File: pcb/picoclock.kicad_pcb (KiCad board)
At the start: 2 copper layers, 175.8 x 64 mm, 58 parts, among them J1 UART, J10 USB, J11 Alt Power, J12 PWM, J2 AUDIO, J3 xx, J4 xx, J6 USB_C_Receptacle, J7 xx, J8 xx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

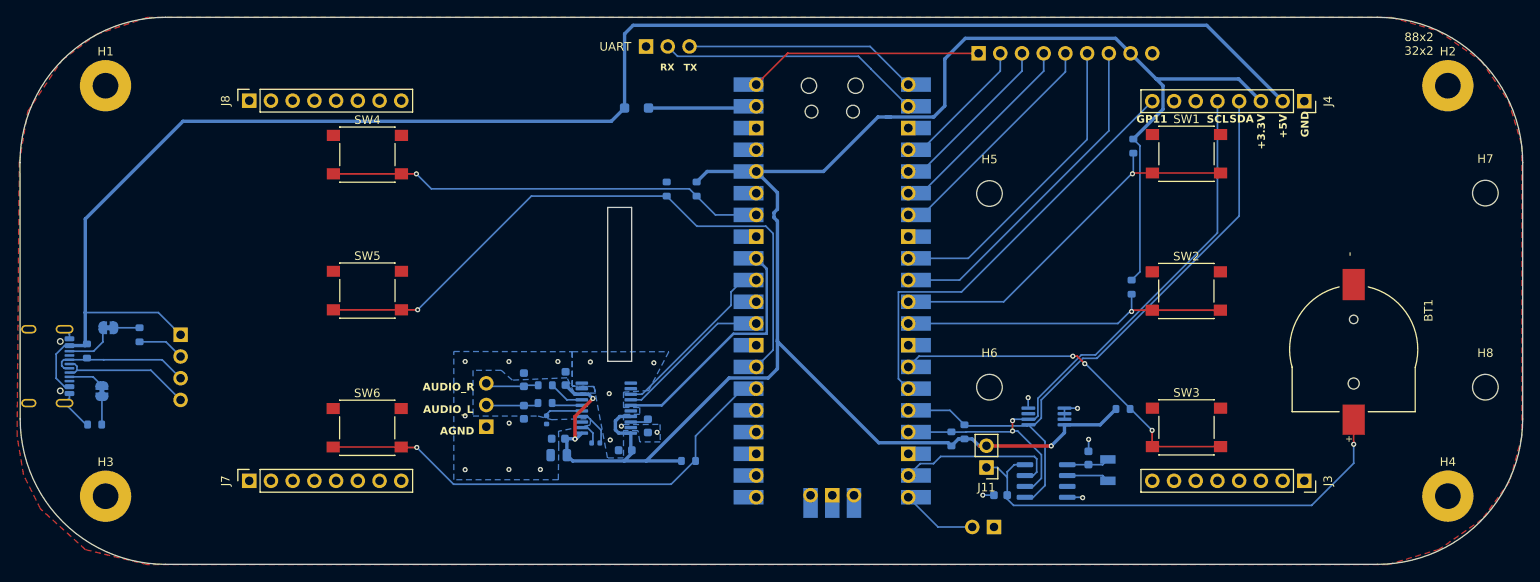
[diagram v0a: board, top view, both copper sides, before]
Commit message: [pcb] new GPIO arrangement
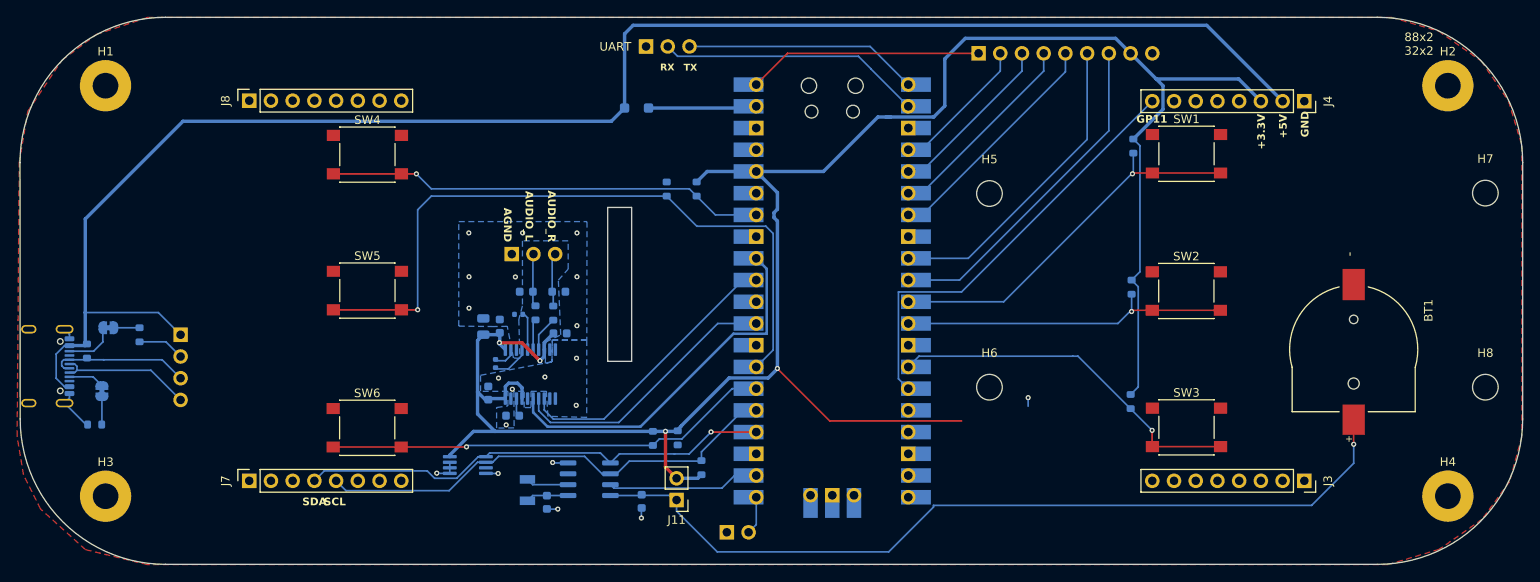
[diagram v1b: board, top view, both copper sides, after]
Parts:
- moved Y1 67.9 mm to (118.2, 122.2), turned to 90 degrees
- moved U3 67.9 mm to (111.3, 119.3), turned to 180 degrees
- moved C1 63.5 mm to (120.5, 123.6), turned to 90 degrees
- moved U1 53.4 mm to (125.5, 120.9), turned to 0 degrees
- moved C2 42.0 mm to (131.6, 123.5), turned to -90 degrees
- moved J11 36.4 mm to (135.7, 123.3)
- moved R1 33.5 mm to (135.8, 116.1), turned to -90 degrees
- moved J12 31.3 mm to (141.6, 127.1), turned to -90 degrees
- moved R3 29.4 mm to (138.6, 119.6)
- moved J2 20.4 mm to (116.4, 94.6), turned to -90 degrees
- moved C6 17.4 mm to (113.1, 103.1), turned to 90 degrees
- moved C3 17.4 mm to (113.7, 110.8), turned to -90 degrees
- moved C9 15.9 mm to (116.5, 113.5), turned to 180 degrees
- moved C7 15.0 mm to (114.5, 107.4), turned to -90 degrees
- moved C4 14.8 mm to (115.0, 103.0), turned to -90 degrees
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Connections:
- net GPIO10 renamed GPIO10/btn
- net GPIO11 renamed GPIO11/led
- net GPIO8 renamed GPIO8/btn
- net GPIO9 renamed GPIO9/btn
- J12 pad 2: GPIO15 / PWM -> GPIO16 / PWM
- J4 pad 4: SDA -> unconnected-(J4-Pin_4-Pad4)
- J4 pad 5: SCL -> unconnected-(J4-Pin_5-Pad5)
- J7 pad 4: unconnected-(J7-Pin_4-Pad4) -> SDA
- J7 pad 5: unconnected-(J7-Pin_5-Pad5) -> SCL
- U2 pad 16: SDA -> SD_D0_MISO
- U2 pad 17: SCL -> SD_D3_CS
- U2 pad 19: SQW -> SD_CLK
- U2 pad 20: GPIO15 / PWM -> SD_CMD_MOSI
- U2 pad 21: SD_D0_MISO -> GPIO16 / PWM
- U2 pad 22: SD_D3_CS -> SQW
- U2 pad 24: SD_CLK -> SDA
- U2 pad 25: SD_CMD_MOSI -> SCL
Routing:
- net 3V BATT: track 56.6 -> 100.1 mm
- net +3.3V: track 234.1 -> 255.1 mm, vias 3 -> 4
- net SDA: track 75.1 -> 55.8 mm, vias 0 -> 1
- net SCL: track 72.7 -> 55.8 mm, vias 2 -> 0
- net LRCK: track 28.7 -> 43.4 mm
- net DIN: track 18.4 -> 32.2 mm
- net BCK: track 21.1 -> 33.3 mm
- net GPIO15 / PWM: track 8.93 -> 0.00 mm
- net GPIO21/btn: track 75.4 -> 82.2 mm
- net GPIO20/btn: track 57.5 -> 52.3 mm
- net GPIO16 / PWM: track 0.00 -> 4.47 mm
- net SD_D3_CS: track 1.19 -> 0.00 mm
- net GND: track 20.3 -> 21.4 mm, vias 19 -> 20
- net GPIO10/btn: vias 3 -> 1

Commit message: [pcb] add sdcard, audio amplifier
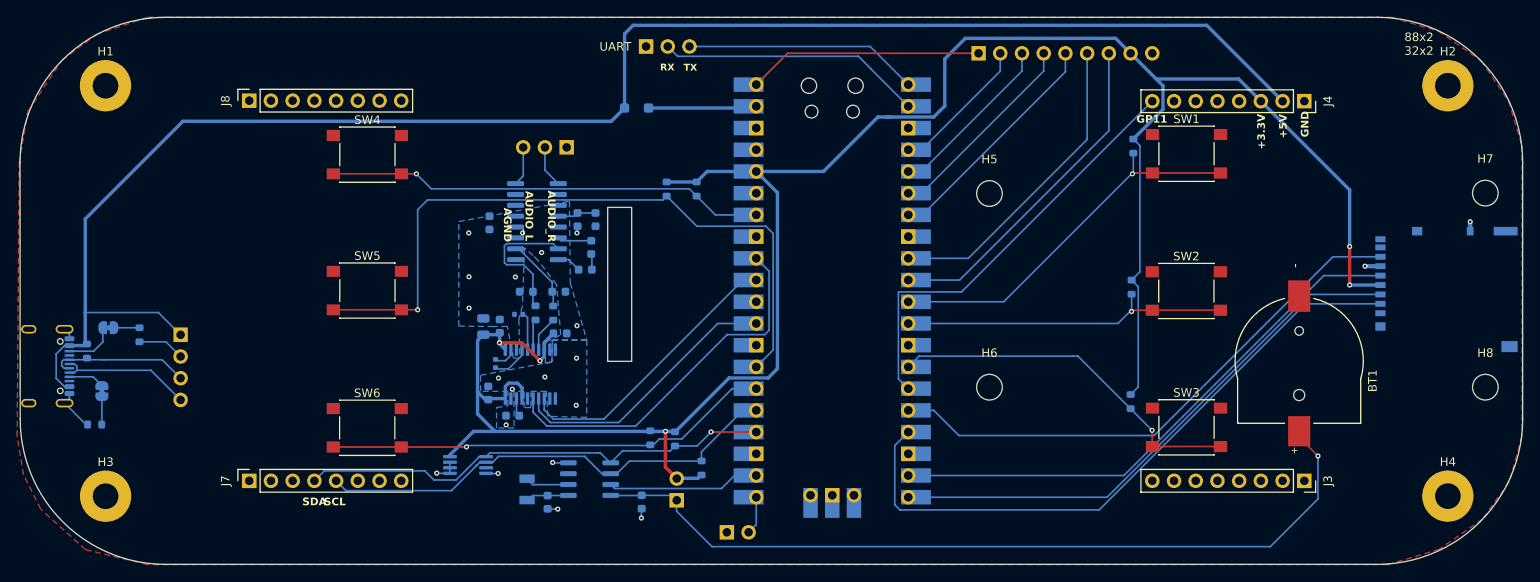
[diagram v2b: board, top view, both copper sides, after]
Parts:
- added C12: 0.1uF, Capacitor_SMD:C_0603_1608Metric, B.Cu at (125.0, 96.4)
- added C13: 1uF, Capacitor_SMD:C_0603_1608Metric, B.Cu at (125.7, 93.8)
- added C14: 1uF, Capacitor_SMD:C_0603_1608Metric, B.Cu at (113.8, 90.9)
- added C15: 1uF, Capacitor_SMD:C_0603_1608Metric, B.Cu at (126.2, 90.5)
- added C16: 470uF, Capacitor_SMD:C_0603_1608Metric, B.Cu at (124.1, 90.5)
- added J5: Micro_SD_Card_Det1, Connector_Card:microSD_HC_Hirose_DM3AT-SF-PEJM5, B.Cu at (225.7, 98.7)
- added U5: PAM8403D, Package_SO:SOP-16_3.9x9.9mm_P1.27mm, B.Cu at (119.3, 90.8)
- J11: moved to B.Cu
- moved J2 14.0 mm to (122.8, 82.1), turned to 90 degrees
- moved BT1 6.52 mm to (208.5, 107.1)
- moved R1 0.33 mm to (135.5, 116.2)
- moved R11 0.32 mm to (132.6, 116.1)
- moved Y1 0.09 mm to (118.2, 122.1)
- moved C1 0.09 mm to (120.6, 123.6)
- moved C2 0.08 mm to (131.6, 123.6)
- turned J11 to 0 degrees
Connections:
- C10 pad 2: WTAUDIO_L -> LINE_OUT_LEFT
- C11 pad 2: WTAUDIO_R -> LINE_OUT_RIGHT
- R2 pad 2: WTAUDIO_L -> LINE_OUT_LEFT
- R4 pad 2: WTAUDIO_R -> LINE_OUT_RIGHT
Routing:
- net SD_D3_CS: track 0.00 -> 76.2 mm
- net SD_D0_MISO: track 0.00 -> 65.4 mm
- net SD_CMD_MOSI: track 0.00 -> 65.0 mm
- net SD_CLK: track 0.00 -> 64.9 mm
- net LINE_OUT_LEFT: track 0.00 -> 16.7 mm
- net +3.3V: track 255.1 -> 265.5 mm, vias 4 -> 5
- net LINE_OUT_RIGHT: track 0.00 -> 8.74 mm
- net Net-(C14-Pad1): track 0.00 -> 4.51 mm
- net Net-(U5-VDD): track 0.00 -> 3.99 mm
- net 3V BATT: track 100.1 -> 97.2 mm
- net Net-(U5-VREF): track 0.00 -> 2.86 mm
- net GND: track 21.4 -> 23.6 mm, vias 20 -> 21
- net WTAUDIO_R: track 6.27 -> 4.61 mm
- net WTAUDIO_L: track 6.14 -> 4.89 mm

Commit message: [pcb] update
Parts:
- added J13: AUDIO, Connector_PinHeader_2.54mm:PinHeader_1x02_P2.54mm_Vertical, F.Cu at (128.3, 84.7)
- added J14: SUPPORT, Connector_PinHeader_2.54mm:PinHeader_1x02_P2.54mm_Vertical, B.Cu at (184.8, 98.8)
- added R14: 470, Resistor_SMD:R_0603_1608Metric, B.Cu at (116.5, 96.2)
- added R15: 470, Resistor_SMD:R_0603_1608Metric, B.Cu at (121.8, 96.2)
- added U6: MCP23009-SO, Package_SO:SSOP-20_5.3x7.2mm_P0.65mm, F.Cu at (154.2, 112.1)
- added U7: MCP4652T, Package_SO:MSOP-10_3x3mm_P0.5mm, B.Cu at (119.1, 94.5)
- J2: footprint Connector_PinHeader_2.54mm:PinHeader_1x03_P2.54mm_Vertical -> Connector_PinHeader_2.54mm:PinHeader_1x02_P2.54mm_Vertical
- moved J2 12.3 mm to (111.2, 85.8), turned to 0 degrees
- moved C4 10.6 mm to (116.8, 113.5), turned to 0 degrees
- moved R3 7.12 mm to (139.9, 112.6), turned to -45 degrees
- moved C15 5.51 mm to (125.6, 85.1)
- moved C16 5.51 mm to (123.5, 85.1)
- moved C12 5.16 mm to (124.4, 91.3)
- moved C13 5.16 mm to (125.1, 88.7)
- moved U5 5.16 mm to (118.7, 85.7)
- moved C9 4.86 mm to (114.0, 109.3), turned to 90 degrees
- moved C14 4.38 mm to (113.9, 86.5)
- moved R10 2.05 mm to (135.3, 85.1), turned to -135 degrees
- moved C3 1.60 mm to (114.0, 112.4), turned to 90 degrees
- moved C6 1.54 mm to (114.6, 102.8)
- moved C10 0.94 mm to (117.2, 99.2)
- moved C11 0.62 mm to (122.5, 99.2)
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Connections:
- J2 pad 1: GND -> AUDIO_OUT_R-
- J2 pad 2: WTAUDIO_L -> AUDIO_OUT_R+
- J4 pad 8: GPIO11/led -> GPIO/led
- U2 pad 15: GPIO11/led -> GPIO11/irq
- U5 pad 1: WTAUDIO_L -> AUDIO_OUT_L+
- U5 pad 10: LINE_OUT_RIGHT -> LOR_ADJ
- U5 pad 12: GND -> MUTE
- U5 pad 14: GND -> AUDIO_OUT_R-
- U5 pad 16: WTAUDIO_R -> AUDIO_OUT_R+
- U5 pad 3: GND -> AUDIO_OUT_L-
- U5 pad 5: GND -> MUTE
- U5 pad 7: LINE_OUT_LEFT -> LOL_ADJ
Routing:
- net SD_DET: track 0.00 -> 92.9 mm, vias 0 -> 1
- net MUTE: track 0.00 -> 60.3 mm, vias 0 -> 1
- net GPIO/led: track 0.00 -> 55.2 mm, vias 0 -> 1
- net SCL: track 55.8 -> 111.0 mm, vias 0 -> 2
- net GPIO11/led: track 50.7 -> 0.00 mm
- net SDA: track 55.9 -> 103.8 mm, vias 1 -> 3
- net +3.3V: track 265.5 -> 288.5 mm, vias 5 -> 6
- net GPIO11/irq: track 0.00 -> 17.0 mm
- net GND: track 23.6 -> 39.0 mm, vias 21 -> 25
- net LINE_OUT_LEFT: track 16.7 -> 4.79 mm
- net GPIO21/btn: track 82.2 -> 91.0 mm
- net AUDIO_OUT_L-: track 0.00 -> 7.79 mm
- net Net-(C14-Pad1): track 4.51 -> 12.3 mm
- net AUDIO_OUT_L+: track 0.00 -> 7.54 mm
- net AUDIO_OUT_R-: track 0.00 -> 5.92 mm
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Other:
- board text added: "DC"
- board text added: "PWR"

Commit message: [pcb] update/fixes for #prod2
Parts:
- added C17: 100nF, Capacitor_SMD:C_0603_1608Metric, F.Cu at (148.7, 107.2)
- added R16: 10K, Resistor_SMD:R_0603_1608Metric, B.Cu at (125.8, 96.2)
- J13: moved to B.Cu
- moved BT1 124.2 mm to (85.1, 93.0)
- moved C2 1.30 mm to (130.3, 123.6)
- moved C12 1.19 mm to (124.1, 90.1)
- moved C13 0.99 mm to (124.1, 88.5), turned to 0 degrees
- turned J13 to 0 degrees
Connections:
- C12 pad 2: +3.3V -> GND
- C13 pad 1: Net-(U5-VDD) -> +3.3V
- C13 pad 2: +3.3V -> GND
- C14 pad 1: Net-(C14-Pad1) -> +3.3V
- C15 pad 1: Net-(C14-Pad1) -> +3.3V
- C16 pad 1: Net-(C14-Pad1) -> +3.3V
- J9 pad 1: PWR -> unconnected-(J9-Pin_1-Pad1)
- U2 pad 40: PWR -> unconnected-(U2-VBUS-Pad40)
- U5 pad 13: Net-(C14-Pad1) -> +3.3V
- U5 pad 4: Net-(C14-Pad1) -> +3.3V
- U5 pad 6: Net-(U5-VDD) -> +3.3V
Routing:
- net PWR: track 27.5 -> 0.00 mm
- net 3V BATT: track 97.2 -> 72.2 mm
- net +3.3V: track 288.5 -> 310.8 mm
- net Net-(C14-Pad1): track 12.3 -> 0.00 mm
- net Net-(U5-VDD): track 3.99 -> 0.00 mm
- net +5V: track 193.8 -> 190.9 mm
- net SD_DET: track 92.9 -> 91.7 mm
- net Net-(U5-VREF): track 2.86 -> 2.09 mm
- net SQW: track 19.1 -> 19.7 mm
- net GND: track 39.0 -> 38.7 mm, vias 25 -> 29
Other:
- board text removed: "AGND"

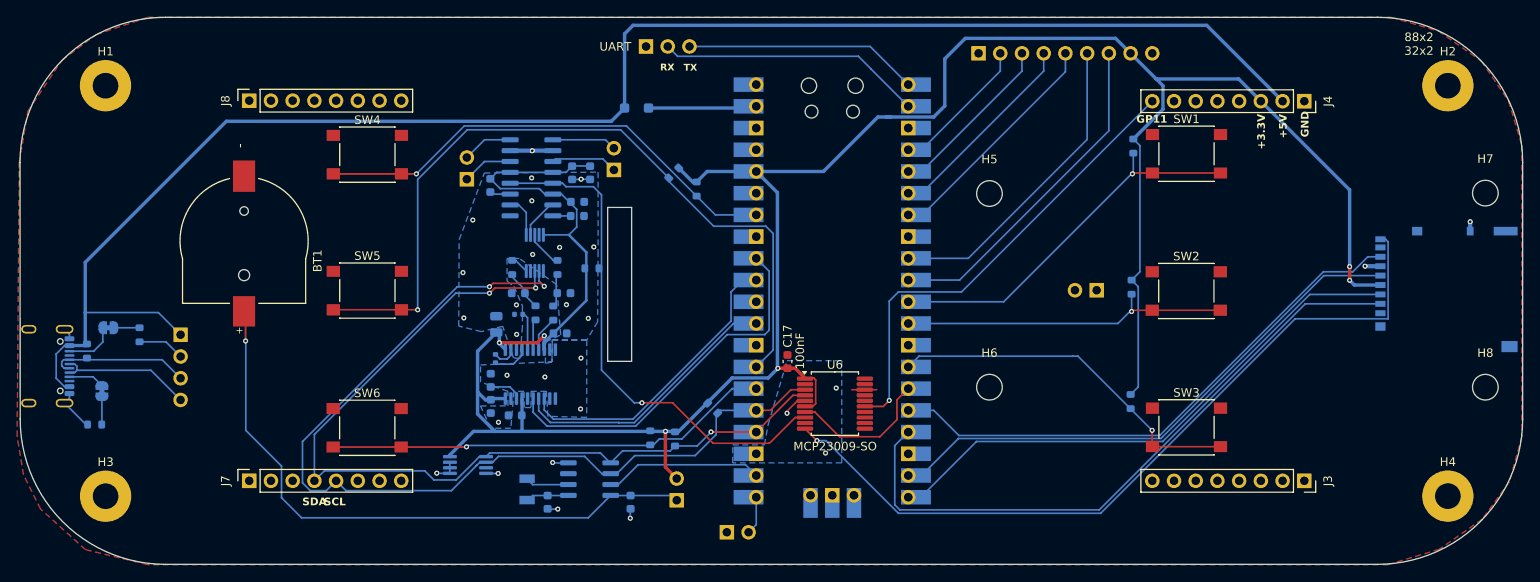
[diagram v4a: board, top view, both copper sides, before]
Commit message: [pcb] move rev2 into dedicated folder + start new rev
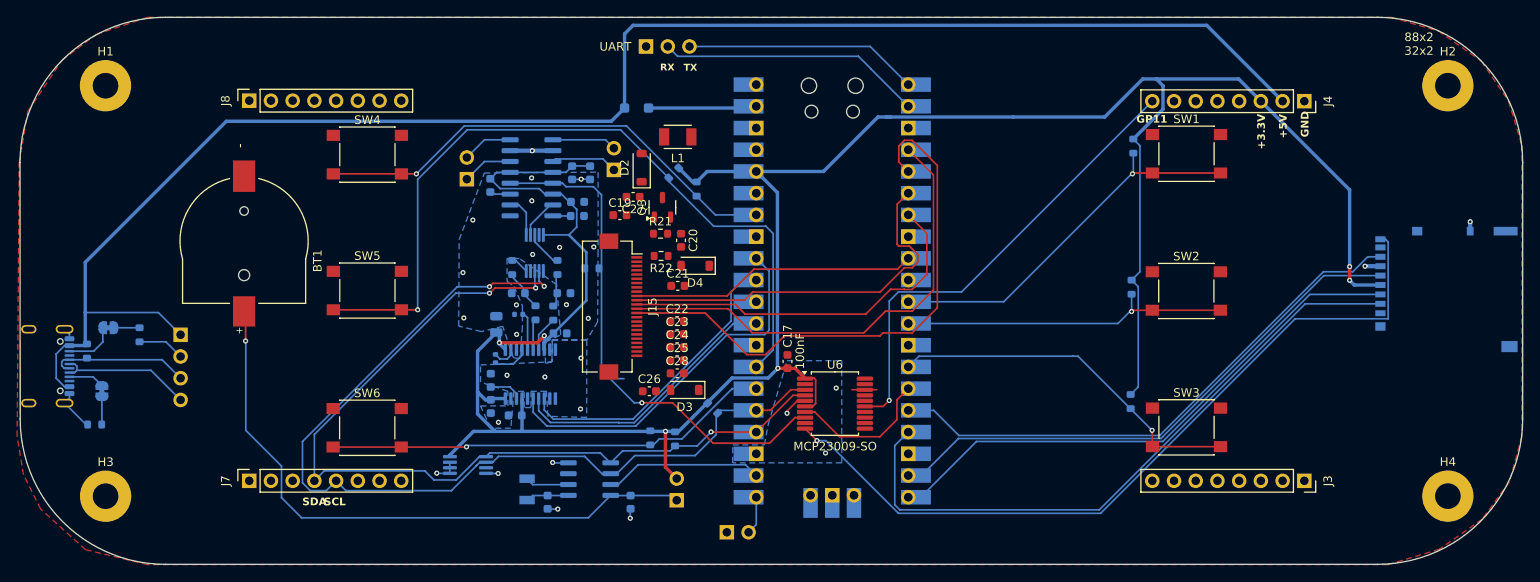
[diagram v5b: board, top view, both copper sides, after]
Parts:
- removed H5, H6, H7, H8: screen_adapter1, MountingHole:MountingHole_3mm
- removed J14: SUPPORT, Connector_PinHeader_2.54mm:PinHeader_1x02_P2.54mm_Vertical
- removed J9: screen_adapter_connector, Connector_PinHeader_2.54mm:PinHeader_1x09_P2.54mm_Vertical
- added C19: 4.7uF, Capacitor_SMD:C_0603_1608Metric, F.Cu at (129.1, 90.0)
- added C20: 4.7uF, Capacitor_SMD:C_0603_1608Metric, F.Cu at (136.2, 93.0)
- added C21: 1uF/25V, Capacitor_SMD:C_0603_1608Metric, F.Cu at (135.8, 98.3)
- added C22: 1uF/10V, Capacitor_SMD:C_0603_1608Metric, F.Cu at (135.8, 102.4)
- added C23: 1uF/10V, Capacitor_SMD:C_0603_1608Metric, F.Cu at (135.8, 104.0)
- added C24: 1uF/25V, Capacitor_SMD:C_0603_1608Metric, F.Cu at (135.8, 105.5)
- added C25: 1uF/25V, Capacitor_SMD:C_0603_1608Metric, F.Cu at (135.8, 107.0)
- added C26: 1uF/25V, Capacitor_SMD:C_0603_1608Metric, F.Cu at (132.5, 110.6)
- added C27: 1uF/25V, Capacitor_SMD:C_0603_1608Metric, F.Cu at (130.6, 87.9)
- added C28: 1uF/25V, Capacitor_SMD:C_0603_1608Metric, F.Cu at (135.8, 108.5)
- added D2: MBR0530, Diode_SMD:D_SOD-123, F.Cu at (131.6, 84.5)
- added D3: MBR0530, Diode_SMD:D_SOD-123, F.Cu at (136.6, 110.5)
- added D4: MBR0530, Diode_SMD:D_SOD-123, F.Cu at (137.8, 96.0)
- added J15: Conn_01x24, Connector_FFC-FPC:Hirose_FH12-24S-0.5SH_1x24-1MP_P0.50mm_Horizontal, F.Cu at (129.2, 100.7)
- added L1: 10uH, Inductor_SMD:L_TDK_NLV32_3.2x2.5mm, F.Cu at (135.8, 80.9)
- added Q3: BSS138, Package_TO_SOT_SMD:SOT-23-3, F.Cu at (134.0, 89.1)
- added R21: 10K, Resistor_SMD:R_0603_1608Metric, F.Cu at (133.8, 92.2)
- added R22: 0.47, Resistor_SMD:R_0603_1608Metric, F.Cu at (133.9, 94.8)
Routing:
- net GPIO3 SPI0 TX: track 20.2 -> 67.1 mm
- net GPIO2 CLK: track 16.7 -> 57.1 mm
- net GPIO5 SCREEN BUSY: track 39.8 -> 0.00 mm
- net GPIO4 DC: track 23.8 -> 46.6 mm
- net GPIO1 SCREEN CS: track 27.5 -> 45.9 mm
- net +3.3V: track 310.8 -> 303.7 mm
- net GPIO1 SCREEN RST: track 36.8 -> 33.6 mm
- net GPIO10/btn: track 42.5 -> 43.1 mm
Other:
- outline, holes or cut-outs redrawn
- board text removed: "PWR"
